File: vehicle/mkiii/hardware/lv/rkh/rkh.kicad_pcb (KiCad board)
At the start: 2 copper layers, 79 x 59.8 mm, 51 parts, among them J10 TWO_WIRE_SCREW_TERMINAL, J3 TWO_WIRE_SCREW_TERMINAL, J4 TWO_WIRE_SCREW_TERMINAL, J6 TWO_WIRE_SCREW_TERMINAL, SW1 CK_KMS2xxGP, U1 Roadkill_MCU, U2 MCP2561-E-SN, U2 MCP6001UT-I/OT, U3 AP63203WU-7

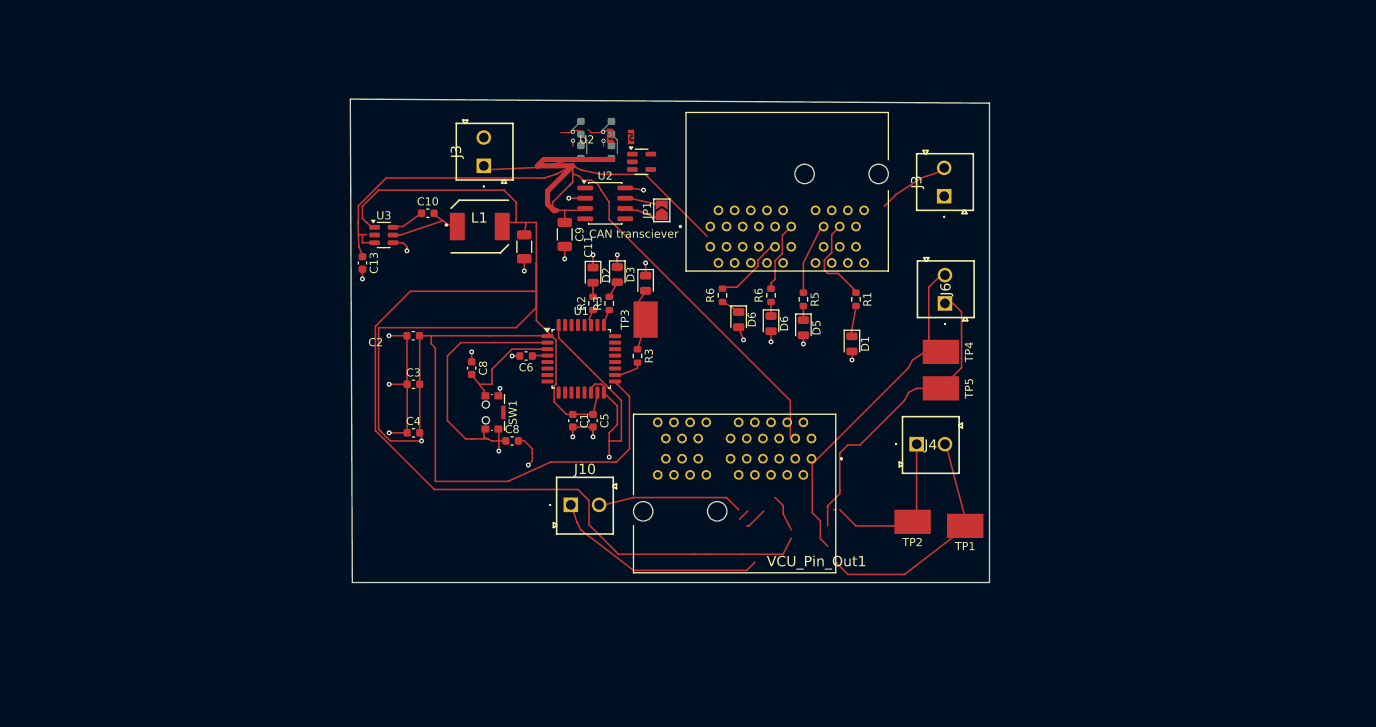
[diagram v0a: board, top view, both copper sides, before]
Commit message: Roadkill Harness Schematics and PCB
authored-by: jackk36 <jgoode736@gmail.com>
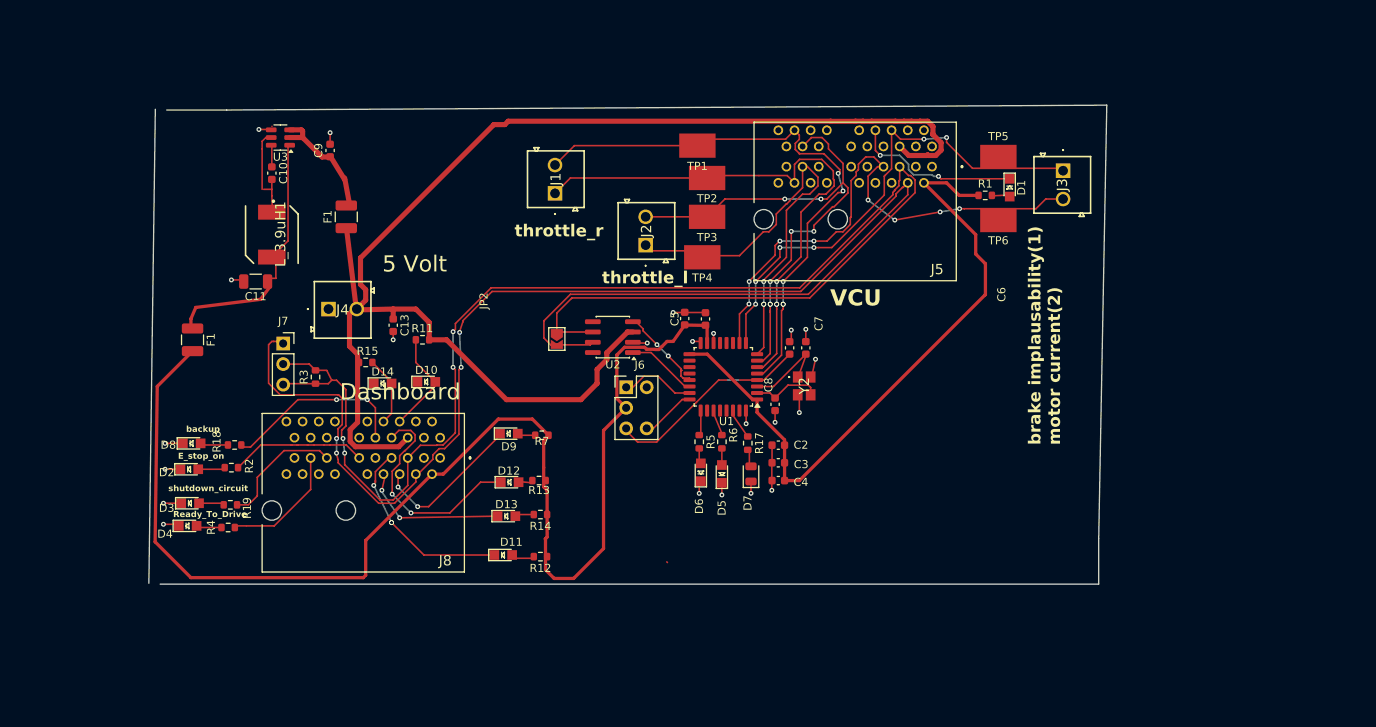
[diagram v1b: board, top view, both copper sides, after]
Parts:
- removed ? (x2): , 
- removed the C8 at (93.5, 107.5)
- removed the C8 at (88.5, 98.5)
- removed the D6 at (125.5, 93.0)
- removed the D6 at (121.5, 92.5)
- removed Dashboard_pinout1, VCU_Pin_Out1: JACK, OEM:J_PCIe_x1
- removed J10: TWO_WIRE_SCREW_TERMINAL, OEM:TAD05021LG
- removed the J3 at (90.0, 73.5)
- removed the J3 at (146.9, 77.2)
- removed JP1: SolderJumper_2_Open, Jumper:SolderJumper-2_P1.3mm_Open_TrianglePad1.0x1.5mm
- removed JP3 (x2): SolderJumper, footprints:SolderJumper-2_Open_Hooks0.8x1.8mm
- removed L1: L_2.2uH_8.2A, OEM:SPM6530 (L_2.2uH_8.2A_19m_SMD - SPM6530T-2R2M)
- removed the R3 at (105.5, 90.5)
- removed the R3 at (109.0, 97.0)
- removed the R6 at (125.5, 89.5)
- removed the R6 at (119.5, 89.5)
- removed the R6 at (102.0, 68.8)
- removed the R6 at (105.8, 68.8)
- removed the R7 at (102.0, 71.8)
- removed the R7 at (105.8, 71.8)
- removed SW1: CK_KMS2xxGP, Button_Switch_SMD:SW_SPST_CK_KMS2xxGP
- removed the U2 at (109.5, 73.0)
- removed the U2 at (105.0, 78.1)
- added C7: 30pf, OEM:C_0603_1608Metric, F.Cu at (129.8, 96.0)
- added C8: 30pF, OEM:C_0603_1608Metric, F.Cu at (126.0, 103.0)
- added D10: LED, OEM:LED_0805_OEM, F.Cu at (82.9, 100.2)
- added D11: LED, OEM:LED_0805_OEM, F.Cu at (92.4, 121.6)
- added D12: LED, OEM:LED_0805_OEM, F.Cu at (93.2, 112.6)
- added D13: LED, OEM:LED_0805_OEM, F.Cu at (92.8, 116.8)
- added D14: LED, OEM:LED_0805_OEM, F.Cu at (77.5, 100.4)
- added D6: LED_break_implausability_if_on, OEM:LED_0805_OEM, F.Cu at (116.8, 111.4)
- added D7: LED_Throttle_Issue_If_On, OEM:D_0805_2012Metric, F.Cu at (123.0, 111.6)
- added D8: LED, OEM:LED_0805_OEM, F.Cu at (53.9, 107.8)
- added D9: LED, OEM:LED_0805_OEM, F.Cu at (93.1, 106.6)
- added F1: F_500mA_16V, OEM:Fuse_1210_3225Metric, F.Cu at (54.0, 95.0)
- added F1: F_500mA_16V, OEM:Fuse_1210_3225Metric, F.Cu at (73.0, 79.8)
- added J1: TWO_WIRE_SCREW_TERMINAL, OEM:TAD05021LG, F.Cu at (98.8, 76.9)
- added J2: TWO_WIRE_SCREW_TERMINAL, OEM:TAD05021LG, F.Cu at (110.0, 83.3)
- added J3: TWO_WIRE_SCREW_TERMINAL, OEM:TAD05021LG, F.Cu at (161.6, 74.1)
- added J5: VCU_pinout, OEM:J_PCIe_x1, F.Cu at (145.4, 73.6)
- added J7: Conn_01x03_Pin, Connector_PinSocket_2.54mm:PinSocket_1x03_P2.54mm_Vertical, F.Cu at (65.2, 95.5)
- added J8: Dashboard_PCIE, OEM:J_PCIe_x1, F.Cu at (84.6, 109.6)
- added JP2: SolderJumper_2_Open, Jumper:SolderJumper-2_P1.3mm_Open_TrianglePad1.0x1.5mm, F.Cu at (99.0, 94.9)
- added L_3.9uH1: L, OEM:SPM6530 (L_2.2uH_8.2A_19m_SMD - SPM6530T-2R2M), F.Cu at (63.8, 82.0)
- added R11: R_1k_0.1W, OEM:R_0603_1608Metric, F.Cu at (82.4, 95.0)
- added R12: R_1k_0.1W, OEM:R_0603_1608Metric, F.Cu at (97.0, 121.8)
- added R13: R_1k_0.1W, OEM:R_0603_1608Metric, F.Cu at (96.8, 112.4)
- added R14: R_1k_0.1W, OEM:R_0603_1608Metric, F.Cu at (97.0, 116.6)
- added R15: R_1k_0.1W, OEM:R_0603_1608Metric, F.Cu at (75.4, 97.8)
- added R17: R_1k_0.1W, OEM:R_0603_1608Metric, F.Cu at (122.6, 107.8)
- added R18: R_1k_0.1W, OEM:R_0603_1608Metric, F.Cu at (59.2, 108.0)
- added R19: R_1k_0.1W, OEM:R_0603_1608Metric, F.Cu at (58.7, 115.4)
- added R3: R_1k_0.1W, OEM:R_0603_1608Metric, F.Cu at (69.2, 99.6)
- added R4: R_1k_0.1W, OEM:R_0603_1608Metric, F.Cu at (58.4, 118.2)
- added R6: R_1k_0.1W, OEM:R_0603_1608Metric, F.Cu at (119.4, 107.6)
- added R7: R_1k_0.1W, OEM:R_0603_1608Metric, F.Cu at (97.2, 106.8)
- added TP4: TestPoint, OEM:Test_Point_SMD, F.Cu at (117.0, 84.8)
- added TP5: TestPoint, OEM:Test_Point_SMD, F.Cu at (153.6, 72.4)
- added TP6: TestPoint, OEM:Test_Point_SMD, F.Cu at (153.6, 80.2)
- added U2: MCP2561-E-SN, Package_SO:SOIC-8_3.9x4.9mm_P1.27mm, F.Cu at (106.0, 94.7)
- added Y2: X_Crystal_GND24, OEM:FA238160000MBC0 (X_16MHz_18pF_SMD - FA-238_16.0000MB-C0), F.Cu at (129.6, 100.7)
- C13: value C_10uF_10V -> 0u1F
- C5: value C_0.1uF_16V -> C_1uF_25V
- C9: value C_22uF_25V -> C_10uF_10V; footprint OEM:C_1206_3216Metric -> OEM:C_0603_1608Metric
- D1: value ready_to_drive -> LED; footprint OEM:D_0805_2012Metric -> OEM:LED_0805_OEM
- D2: value D_Red_LED -> LED; footprint OEM:D_0805_2012Metric -> OEM:LED_0805_OEM
- D3: value LED_brake_implausability_if_on -> LED; footprint OEM:D_0805_2012Metric -> OEM:LED_0805_OEM
- D4: value LED_Throttle_Issue_If_On -> LED; footprint OEM:D_0805_2012Metric -> OEM:LED_0805_OEM
- D5: value E_stop_on -> LED_Motor_Current_Issue_If_On; footprint OEM:D_0805_2012Metric -> OEM:LED_0805_OEM
- J6: value TWO_WIRE_SCREW_TERMINAL -> J_Programming_Pin_Header; footprint OEM:TAD05021LG -> OEM:J_Programming_Pin_Header_Keyed
- TP1, TP2, TP3: value TP_SMD -> TestPoint; footprint OEM:TP_Hook_SMD -> OEM:Test_Point_SMD
- U1: value Roadkill_MCU -> STM32G441KBT6
- moved J4 74.6 mm to (70.8, 91.2)
- moved D4 64.1 mm to (53.4, 118.0), turned to 0 degrees
- moved D3 59.9 mm to (53.7, 115.2), turned to 0 degrees
- moved TP1 57.5 mm to (116.4, 71.0)
- moved D2 55.4 mm to (53.6, 111.0), turned to 0 degrees
- moved TP2 49.5 mm to (117.6, 75.0)
- moved R2 49.1 mm to (58.8, 110.8), turned to 0 degrees
- moved C2 47.1 mm to (126.4, 108.0)
- moved C3 46.1 mm to (126.4, 110.2)
- moved C4 45.5 mm to (126.4, 112.4)
- moved J6 40.7 mm to (107.6, 100.9), turned to 0 degrees
- moved C11 33.5 mm to (61.8, 87.8), turned to 180 degrees
- moved C6 32.6 mm to (127.8, 96.0), turned to -90 degrees
- moved C9 30.8 mm to (71.0, 71.6), turned to 90 degrees
- moved D1 27.4 mm to (155.0, 76.2)
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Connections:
- C11 pad 1: /3V_buck_converter/V_out(3.3V) -> +3V3
- C13 pad 1: /3V_buck_converter/Vin(5V) -> +5V
- C5 pad 1: (no net) -> +3V3
- C5 pad 2: (no net) -> GND
- C6 pad 1: /NRST -> GND
- C6 pad 2: GND -> /NRST
- C9 pad 1: V_out_5v -> +5V
- C9 pad 2: Earth -> GND
- D1 pad 1: (no net) -> Net-(D1-K)
- D1 pad 2: (no net) -> Net-(D1-A)
- D3 pad 1: (no net) -> GND
- D3 pad 2: (no net) -> Net-(D3-A)
- D5 pad 1: (no net) -> GND
- D5 pad 2: (no net) -> Net-(D5-A)
- J4 pad 1: /brake light connection -> (no net)
- J4 pad 2: unconnected-(J4-Pad2) -> +5V
- J6 pad 1: /throttle1+ -> /SWDIO
- J6 pad 2: /throttle1- -> GND
- R1 pad 1: /Ready_to_drive -> +3V3
- R2 pad 1: Net-(U3-V+) -> /E_stop_on
- R2 pad 2: Net-(U3-V+) -> Net-(D2-A)
- R5 pad 1: /shutdown_circuit_triggered -> Net-(D6-A)
- TP1 pad 1: Net-(U1-SW) -> /throttle_r-
- TP2 pad 1: Net-(U5-SW) -> /throttle_r+
- TP3 pad 1: unconnected-(TP3-Pad1) -> /throttle_l-
- U1 pad 10: unconnected-(U1-(TIM2_ETR/TIM2_CH1/GPIO_EXTI5/ADC2_IN13)PA5*-Pad10) -> /motor_current_sense
- U1 pad 18: Net-(D4-A) -> Net-(U1-(TIM4_ETR/USART1_CK/GPIO_EXTI8)PA8)
- U1 pad 19: unconnected-(U1-(TIM2_CH3/TIM15_BKIN/USART1_TX/GPIO_EXTI9)PA9-Pad19) -> x
- U1 pad 20: unconnected-(U1-(TIM2_CH4/USART1_RX/TIM17_BKIN/GPIO_EXTI10)PA10-Pad20) -> x
- U1 pad 21: unconnected-(U1-(FDCAN1_RX/GPIO_EXTI11)PA11-Pad21) -> /CAN_RX
- U1 pad 22: unconnected-(U1-(FDCAN1_TX/GPIO_EXTI12)PA12-Pad22) -> /CAN_TX
- U1 pad 25: Net-(U1-(TIM2_ETR/TIM2_CH1/GPIO_EXTI15)PA15) (its old number) -> Net-(D6-A)
- U1 pad 27: Net-(U1-(TIM17_BKIN/SPI1_MISO/TIM3_CH1/TIM16_CH1/GPIO_EXTI4)PB4) -> Net-(D5-A)
- U1 pad 28: unconnected-(U1-(TIM17_CH1/SPI1_MOSI/TIM3_CH2/TIM16_BKIN/GPIO_EXTI5)PB5-Pad28) -> x
- U1 pad 29: unconnected-(U1-(TIM4_CH1/TIM16_CH1N/GPIO_EXTI6)PB6-Pad29) -> x
- U1 pad 30: unconnected-(U1-(TIM3_CH4/TIM4_CH2/TIM17_CH1N/GPIO_EXTI7)PB7-Pad30) -> Net-(D7-A)
- U1 pad 31: unconnected-(U1-(TIM4_CH3/TIM16_CH1/GPIO_EXTI8)PB8-BOOT0-Pad31) -> x
- U1 pad 5: unconnected-(U1-(TIM2_ETR/TIM2_CH1/GPIO_EXTI0/ADC2_IN1/ADC1_IN1)PA0*-Pad5) -> /throttle_r-
- U1 pad 6: unconnected-(U1-(TIM15_CH1N/TIM2_CH2/GPIO_EXTI1/ADC2_IN2/ADC1_IN2)PA1*-Pad6) -> /throttle_r+
- U1 pad 7: unconnected-(U1-(TIM15_CH1/USART2_TX/TIM2_CH3/GPIO_EXTI2/ADC1_IN3)PA2*-Pad7) -> /throttle_l-
- U1 pad 8: unconnected-(U1-(TIM15_CH2/USART2_RX/TIM2_CH4/GPIO_EXTI3/ADC1_IN4)PA3*-Pad8) -> /throttle_l+
- U1 pad 9: unconnected-(U1-(USART2_CK/TIM3_CH2/GPIO_EXTI4/ADC2_IN17)PA4*-Pad9) -> /break_pressure_sensor
- U3 pad 1: /3V_buck_converter/V_out(3.3V) -> +3V3
- U3 pad 2: /3V_buck_converter/Vin(5V) -> +5V
- U3 pad 3: /3V_buck_converter/Vin(5V) -> +5V
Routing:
- net /CAN_-: track 0.00 -> 178.3 mm, vias 0 -> 4
- net /CAN_+: track 0.00 -> 175.4 mm, vias 0 -> 4
- net +5V: track 5.43 -> 164.9 mm
- net +3V3: track 127.8 -> 243.3 mm, vias 1 -> 0
- net unconnected-(Dashboard_pinout1-3.3V-PadA2): track 81.6 -> 0.00 mm
- net /throttle_r-: track 0.00 -> 65.5 mm, vias 0 -> 5
- net /throttle_r+: track 0.00 -> 62.5 mm, vias 0 -> 3
- net /throttle_l-: track 0.00 -> 53.2 mm, vias 0 -> 7
- net /throttle_l+: track 0.00 -> 50.6 mm, vias 0 -> 3
- net /break_pressure_sensor: track 0.00 -> 50.2 mm, vias 0 -> 6
- net /motor_current_sense: track 0.00 -> 45.4 mm, vias 0 -> 8
- net unconnected-(VCU_Pin_Out1-5V-PadB5): track 39.9 -> 0.00 mm
- net GND: track 46.4 -> 10.5 mm, vias 19 -> 22
- net Net-(U1-SW): track 29.5 -> 0.00 mm
- net unconnected-(VCU_Pin_Out1-io_19-PadB15): track 27.7 -> 0.00 mm
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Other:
- board size 79 x 59.8 mm -> 118.4 x 59.2 mm
- board text added: "5 Volt"
- board text added: "AP63203WU-7"
- board text added: "Brake_Implausability"
- board text added: "C6"
- board text added: "Dashboard"
- board text added: "E_stop_on"
- board text added: "JP2"
- board text added: "Motor_current"
- board text added: "R18"
- board text added: "Ready_To_Drive"
- board text added: "VCU"
- board text added: "backup"
- board text added: "brake implausability(1) motor current(2)"
- board text added: "shutdown_circuit"
- board text added: "throttle_l"
- board text added: "throttle_r"
- board text removed: "5 Volts"
- board text removed: "Brake_pressor(1) brakelight_conn(2)"
- board text removed: "Brakelight_conn(2)"
- board text removed: "C8"
- board text removed: "CAN transciever"
- board text removed: "D1"
- board text removed: "D4"
- board text removed: "LED_Motor_Current_Issue_If_On"
- board text removed: "TP4"
- board text removed: "TP5"
- board text removed: "buck converter v2"
- board text removed: "circuit_"
- board text removed: "connection"
- board text removed: "triggered"

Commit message: Roadkill Harness - fixed ERC issues. Replaced shutdown circuit with LEDs to indicate if shutdown circuit is on
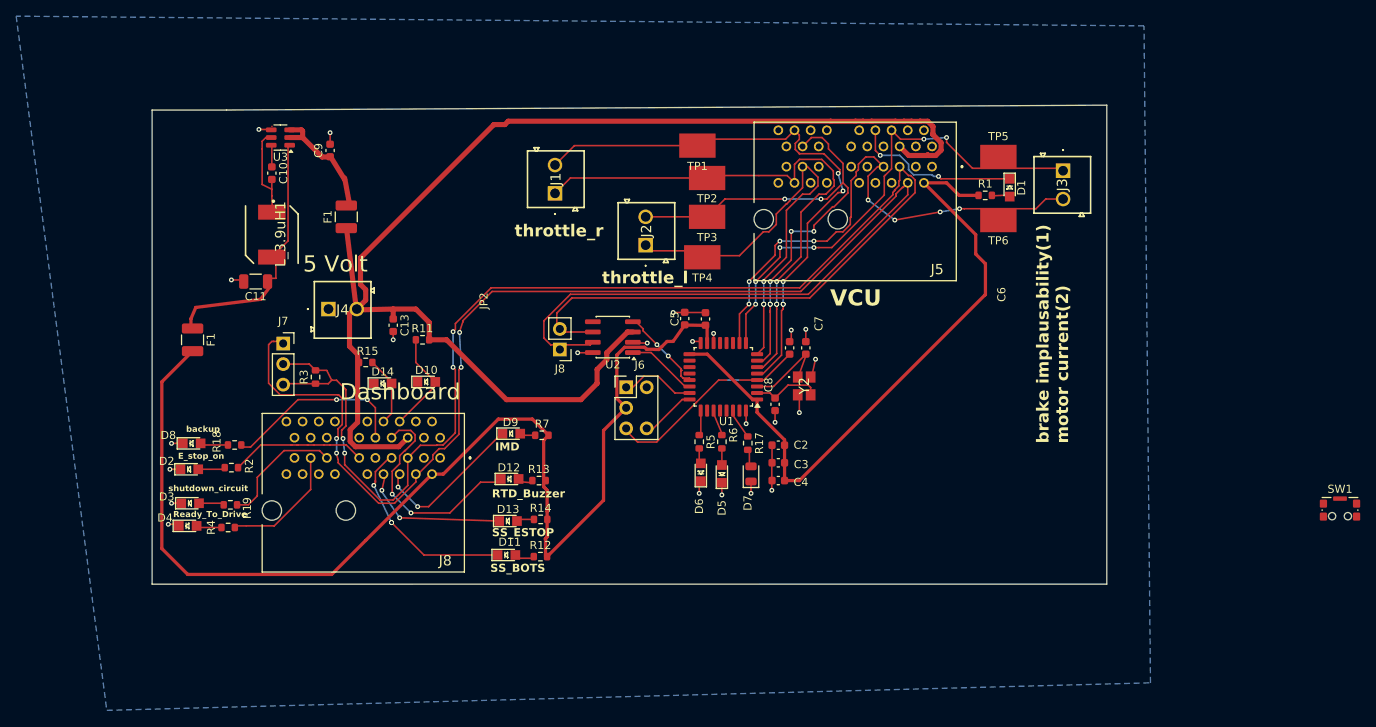
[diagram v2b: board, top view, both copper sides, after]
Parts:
- removed JP2: SolderJumper_2_Open, Jumper:SolderJumper-2_P1.3mm_Open_TrianglePad1.0x1.5mm
- added J8: Conn_01x02_Pin, Connector_PinHeader_2.54mm:PinHeader_1x02_P2.54mm_Vertical, F.Cu at (99.4, 96.2)
- added SW1: CK_KMS2xxG, Button_Switch_SMD:SW_SPST_CK_KMS2xxGP, F.Cu at (195.8, 116.0)
- moved D13 0.63 mm to (93.0, 117.4)
- moved R14 0.60 mm to (97.0, 117.2)
- moved D11 0.40 mm to (92.8, 121.6)
- moved D12 0.40 mm to (93.2, 112.2)
- moved D9 0.30 mm to (93.4, 106.6)
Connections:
- D13 pad 1: unconnected-(D13-K-Pad1) -> Net-(D13-K)
- R11 pad 1: +5V -> +3V3
- R15 pad 1: +5V -> +3V3
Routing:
- net +3V3: track 243.3 -> 232.9 mm
- net GND: track 10.5 -> 7.96 mm, vias 22 -> 23
- added copper zone on B.Cu, net GND
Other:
- board size 118.4 x 59.2 mm -> 118 x 59.2 mm
- board text added: "IMD"
- board text added: "RTD_Buzzer"
- board text added: "SS_BOTS"
- board text added: "SS_ESTOP"

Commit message: Updated shutdown circuit from parallel to series. Added voltage divider for brake_pressure and motor_current sensors, reducing the volts they deliver to the STM32.  Removed unecessary dashboard LEDs
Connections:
- R11 pad 1: +3V3 -> +5V
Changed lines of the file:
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@@
 			(layers "F.Cu" "F.Mask" "F.Paste")
 			(roundrect_rratio 0.25)
-			(net 2 "+3V3")
+			(net 25 "+5V")
 			(pintype "passive")
 		)
